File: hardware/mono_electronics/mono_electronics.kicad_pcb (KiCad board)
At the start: 4 copper layers, 190 x 148 mm, 181 parts, among them SW1 KMR2, U1 ESP32-S3FN8, Y1 L327S400H11L

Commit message: fix(mono): AON spine connectivity, VBUS decouple, DRC 0/0/73
- Join MCU AON east spine to translator bus on In2 to avoid ROW_01_Y crossing
  and prevent orphaned In1 stub from merging into GND on save.
- Route C_USB1 VBUS to existing USB In2 spine.
- Add drc_summary.py helper; document findings in LAST_CHANGES and cursor.md.

Co-authored-by: illiapliukhin <illiapliukhin@users.noreply.github.com>
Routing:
- net AON_3V3: track 98.6 -> 173.6 mm, vias 6 -> 10
- net GND: track 989.8 -> 915.7 mm, vias 52 -> 49
- net VBUS: track 50.0 -> 58.0 mm, vias 5 -> 6

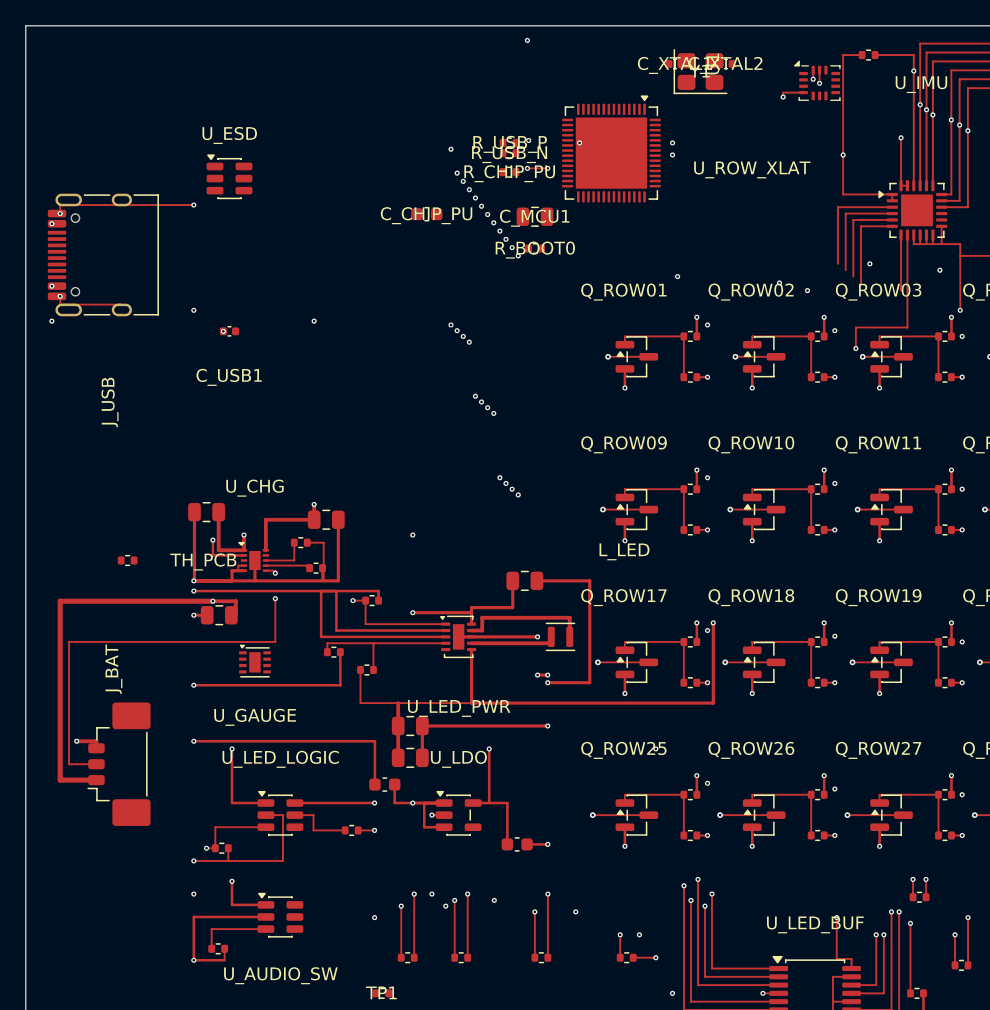
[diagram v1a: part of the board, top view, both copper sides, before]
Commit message: feat(mono): ESP32 pad remap, A* MCU grid router, 0-short grid pass
- Fix U1 pad map (SPICS0/GPIO6 NC; ROW_A0–A2 and AUDIO_EN GPIO remap)
- Remove illegal AON via in EP; placement for Y1/USB/crystal courtyards
- Add mcu_grid pipeline (dump → A* compute → apply complete nets only)
- Regenerated mono_electronics: 0 shorts/crossings, 46 unconnected with grid

Co-authored-by: illiapliukhin <illiapliukhin@users.noreply.github.com>
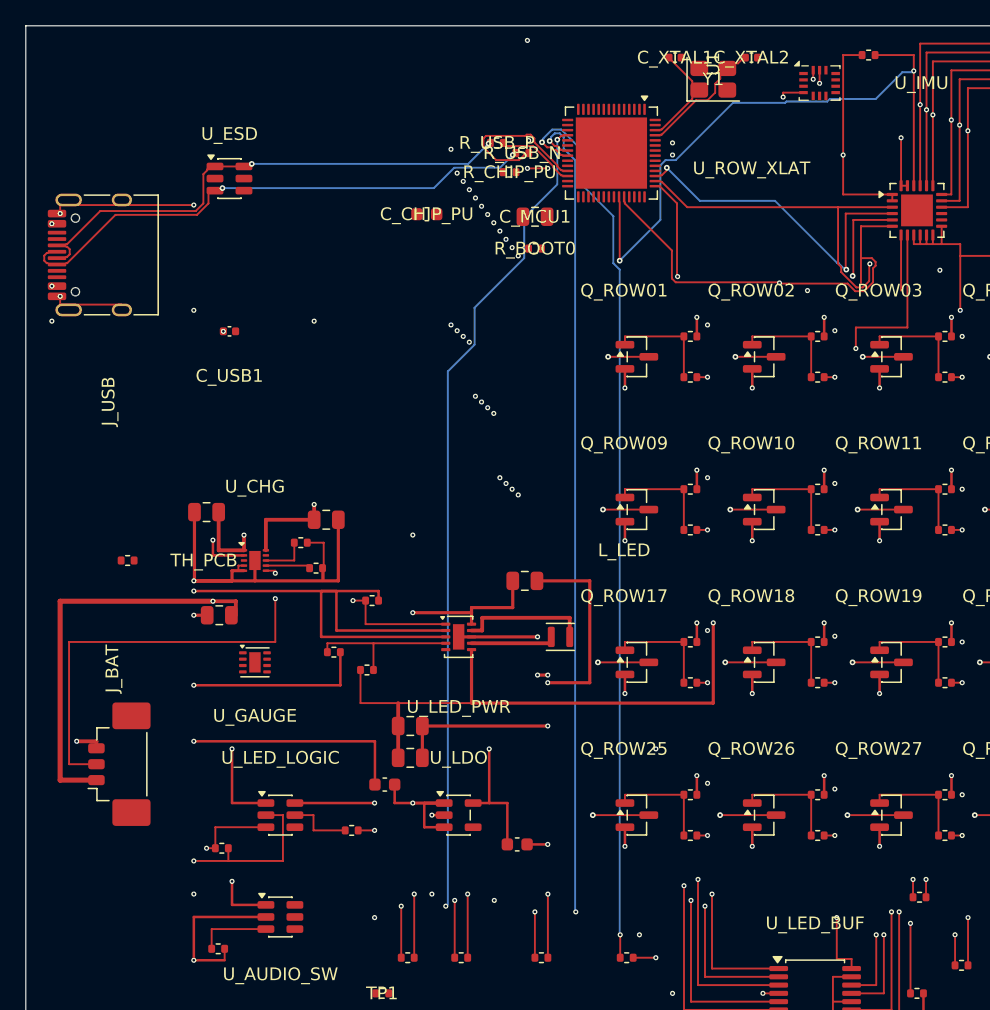
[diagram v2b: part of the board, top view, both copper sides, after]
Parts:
- moved C_XTAL2 2.06 mm to (57.0, 2.50)
- moved Y1 1.17 mm to (54.0, 4.20)
- moved R_USB_N 1.00 mm to (39.0, 10.0)
- moved R_USB_P 1.00 mm to (37.0, 9.20)
- moved C_XTAL1 0.50 mm to (51.0, 2.50)
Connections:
- U1 pad 11: GND -> (no net)
- U1 pad 23: ROW_A0 -> AUDIO_EN
- U1 pad 24: ROW_A1 -> (no net)
- U1 pad 27: ROW_A2 -> (no net)
- U1 pad 32: GND -> (no net)
- U1 pad 43: (no net) -> ROW_A2
- U1 pad 44: GND -> ROW_A0
- U1 pad 45: GND -> ROW_A1
- U1 pad 48: AUDIO_EN -> (no net)
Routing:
- net LED_OE_N: track 64.7 -> 133.7 mm, vias 5 -> 6
- net LED_CLK: track 68.1 -> 132.3 mm, vias 4 -> 5
- net LED_LE: track 77.6 -> 141.6 mm, vias 5 -> 6
- net USB_D_N: track 0.00 -> 38.9 mm, vias 0 -> 2
- net USB_D_P: track 0.00 -> 36.5 mm, vias 0 -> 2
- net ROW_XLAT_OE_N: track 156.0 -> 192.2 mm, vias 3 -> 4
- net ROW_A3: track 133.0 -> 159.6 mm
- net ROW_A0: track 92.8 -> 112.3 mm
- net ROW_A1: track 100.6 -> 118.6 mm, vias 2 -> 4
- net USB_D_N_MCU: track 0.00 -> 12.3 mm
- net XTAL_N: track 0.00 -> 7.86 mm
- net ROW_A2: track 135.9 -> 143.3 mm, vias 2 -> 3
- net AON_3V3: track 173.6 -> 166.3 mm, vias 10 -> 9
- net XTAL_P: track 0.00 -> 6.16 mm
- net USB_D_P_MCU: track 0.00 -> 5.41 mm

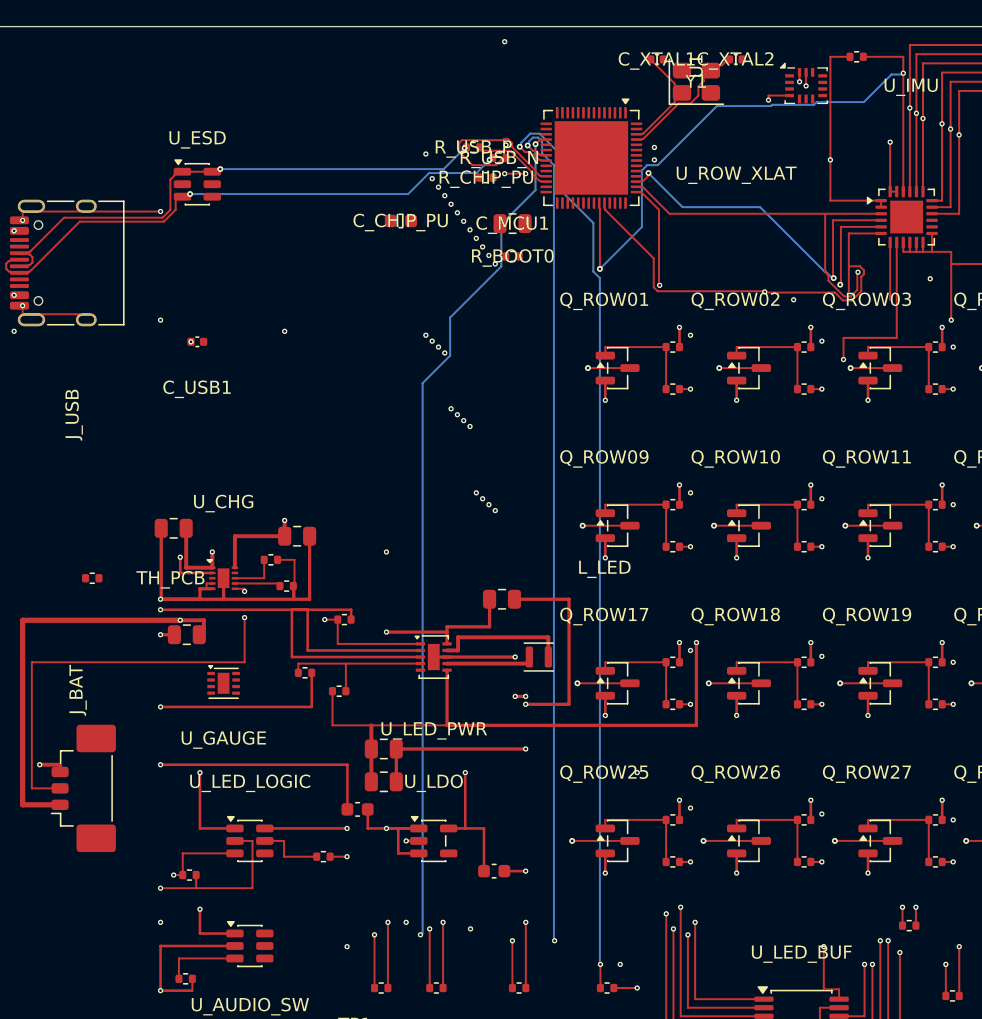
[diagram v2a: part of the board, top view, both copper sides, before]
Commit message: feat(mono): PathFinder grid negotiation and GND mesh helpers
Add pathfinder.py (history/rip-up/finish pass) behind MONO_PATHFINDER=1;
keep greedy router as default for 0-short apply. Extend grid Board with
recommit/uncommit and power track width. GND stitch/B.Cu mesh optional
(add_gnd_mesh false). Regenerated mono_electronics at 0/0/45 unconnected.

Co-authored-by: illiapliukhin <illiapliukhin@users.noreply.github.com>
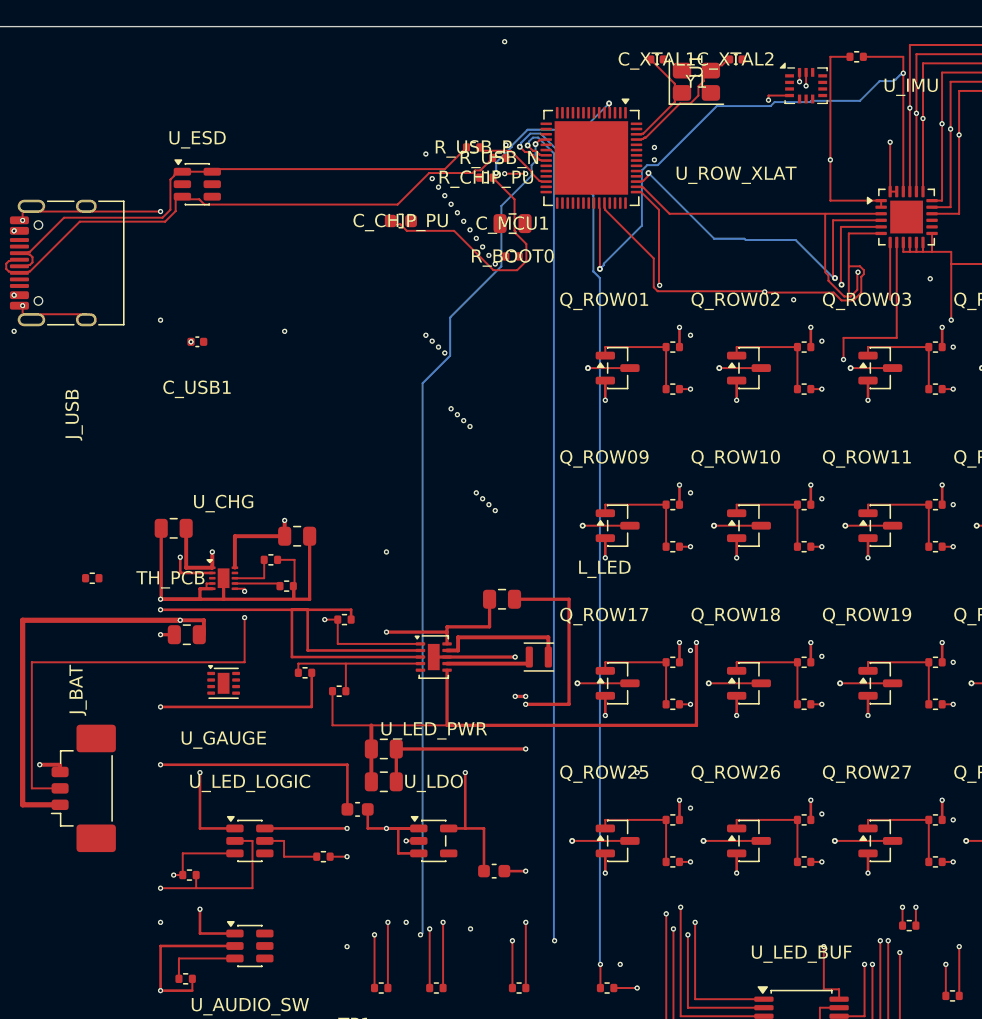
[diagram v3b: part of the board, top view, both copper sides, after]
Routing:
- net CHIP_PU: track 0.00 -> 30.4 mm, vias 0 -> 2
- net USB_D_N_MCU: track 12.3 -> 0.00 mm
- net USB_D_N: track 38.9 -> 39.4 mm, vias 2 -> 0
- net USB_D_P: track 36.5 -> 36.3 mm, vias 2 -> 0

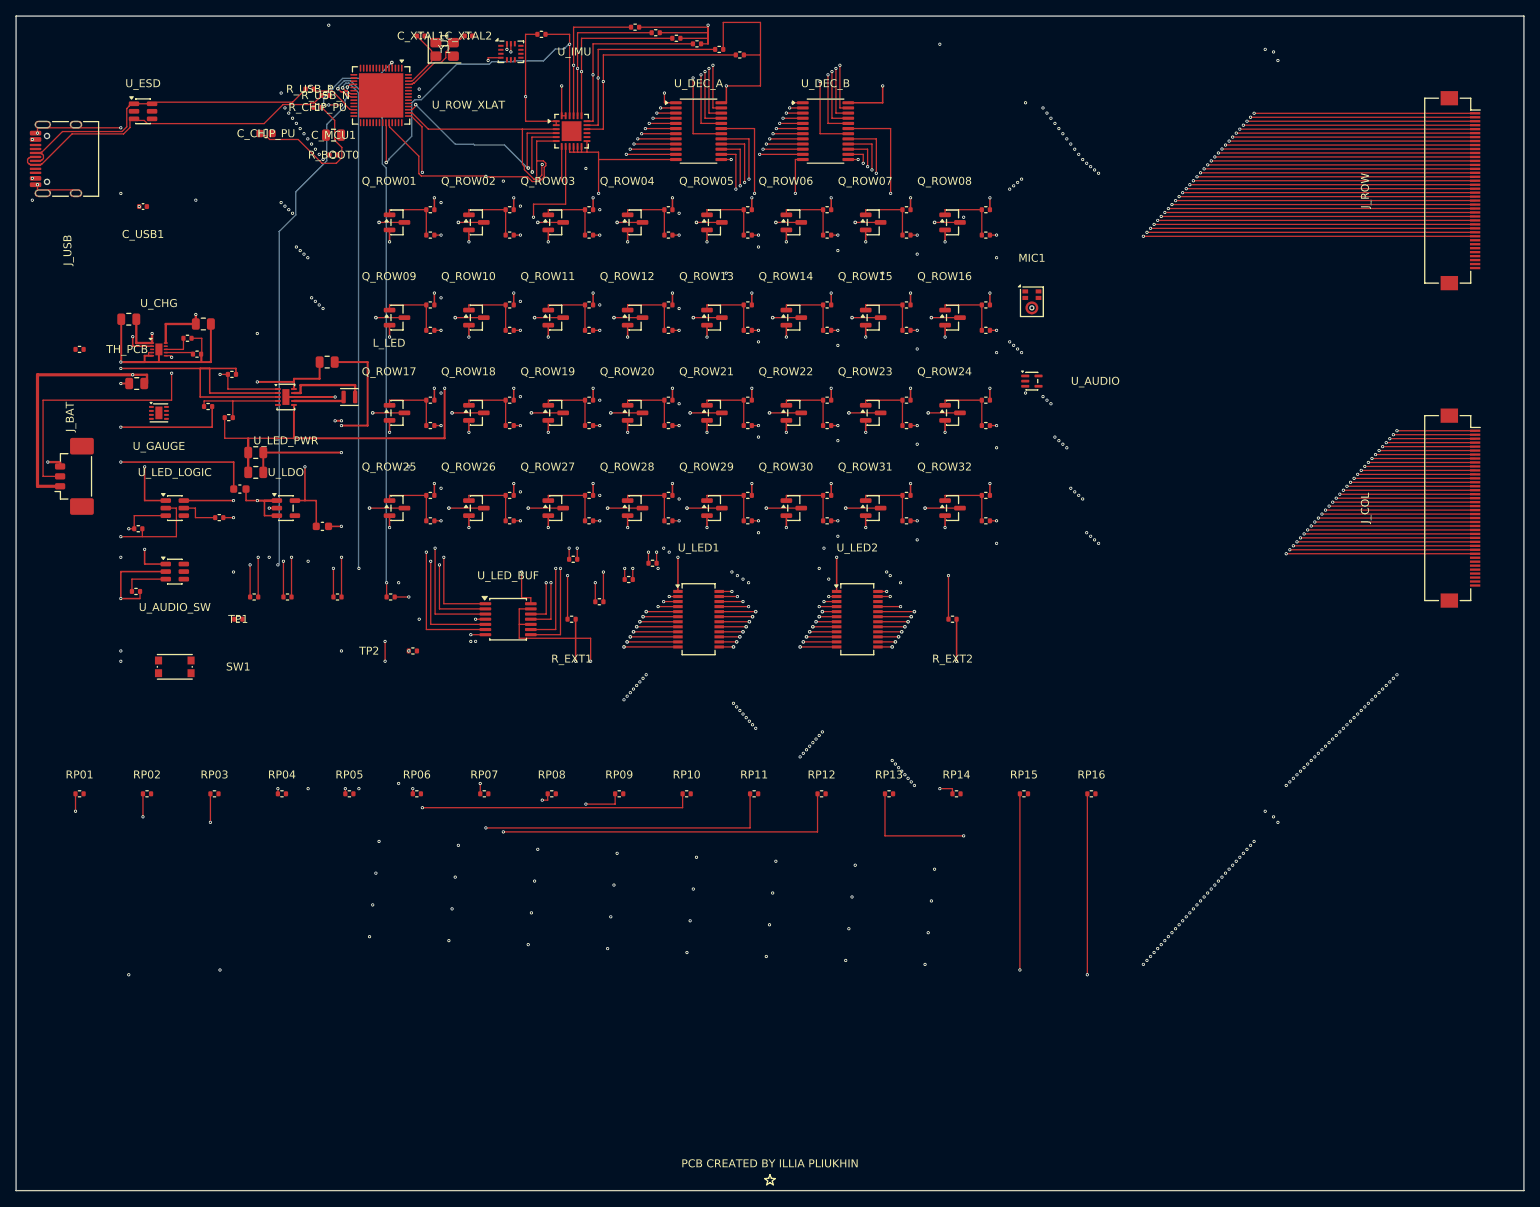
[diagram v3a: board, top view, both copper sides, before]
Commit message: feat(mono): PathFinder-first MCU grid with GPIO remap and GND refill
Run greedy and PathFinder compute, apply PathFinder when DRC gate passes
(0 shorts, 0 crossings) with more complete nets than greedy. Remap stubborn
nets to west/east pads (GPIO6/18/21/41/42), adjust USB series placement, add
In2/B GND zones filled via kicad-cli, and document the updated pin map.

Co-authored-by: illiapliukhin <illiapliukhin@users.noreply.github.com>
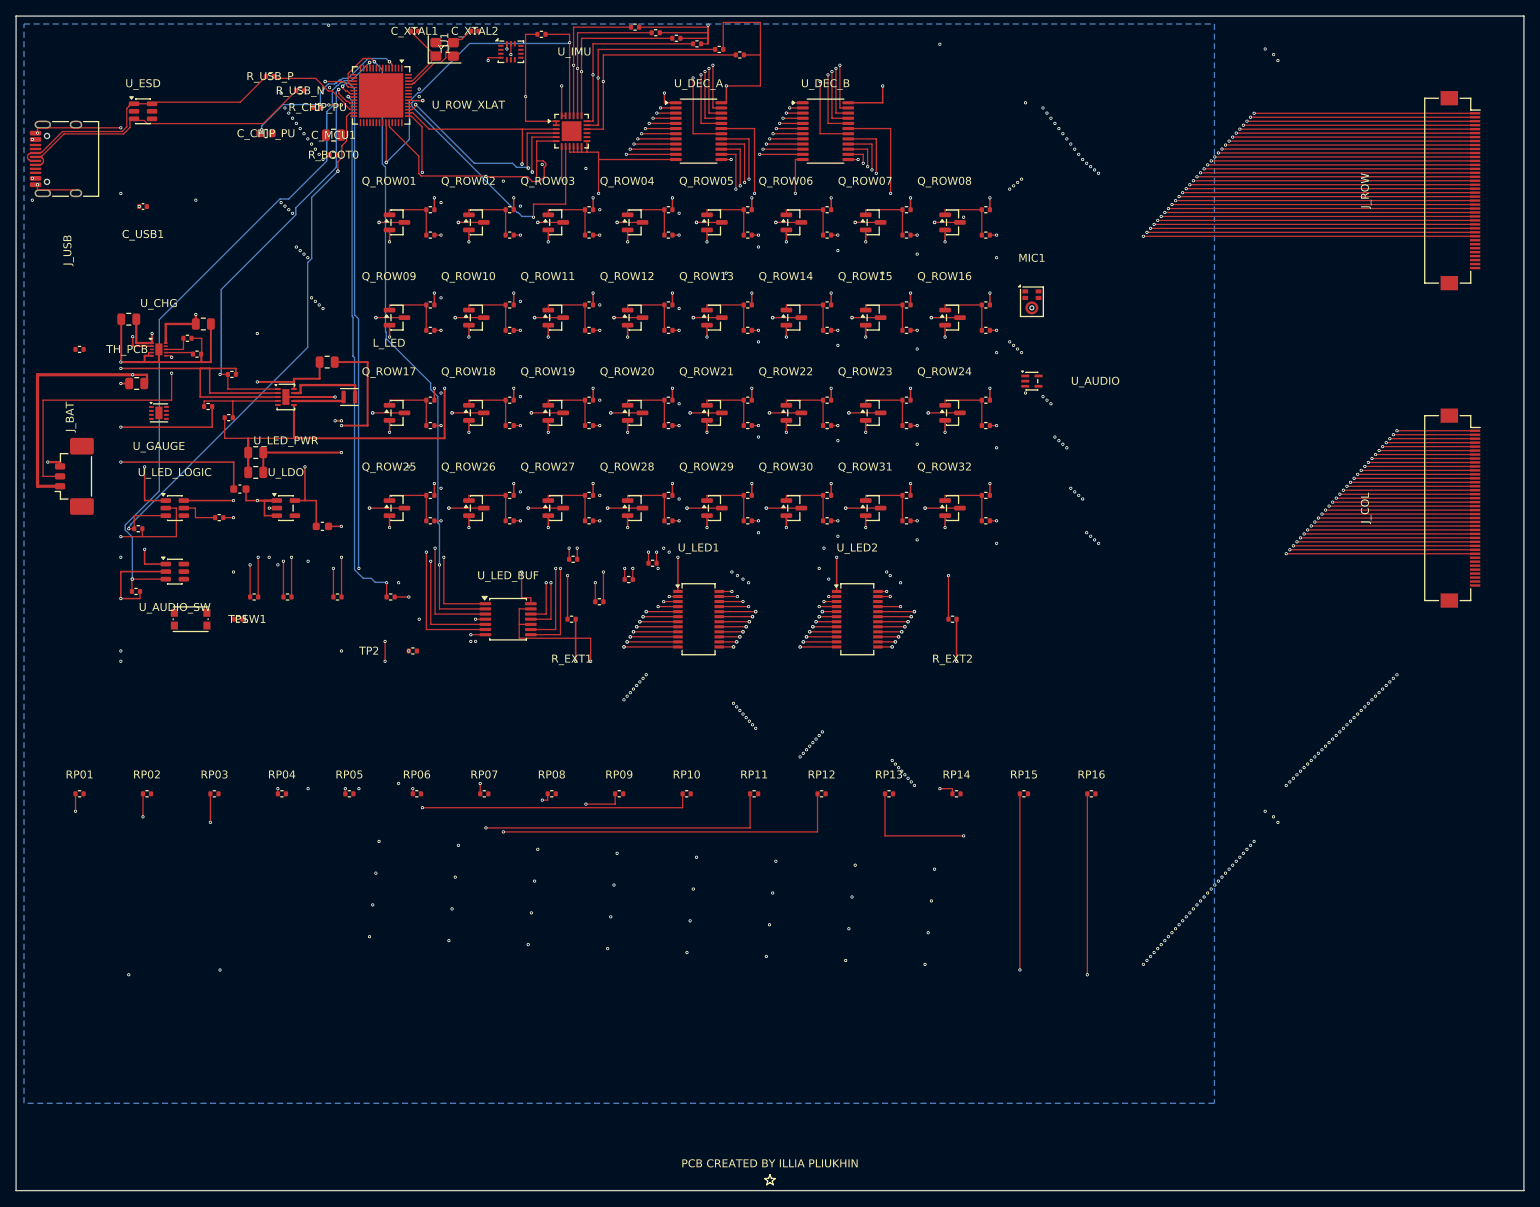
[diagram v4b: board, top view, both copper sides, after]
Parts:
- moved SW1 6.32 mm to (22.0, 76.0)
- moved R_USB_P 5.25 mm to (32.0, 7.60)
- moved R_USB_N 3.26 mm to (35.8, 9.40)
- moved C_XTAL1 1.00 mm to (50.2, 1.90)
- moved C_XTAL2 1.00 mm to (57.8, 1.90)
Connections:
- U1 pad 11: (no net) -> AUDIO_EN
- U1 pad 23: AUDIO_EN -> (no net)
- U1 pad 24: (no net) -> LED_EN
- U1 pad 27: (no net) -> LED_LOGIC_EN
- U1 pad 39: DEC_A_EN_N -> (no net)
- U1 pad 40: DEC_B_EN_N -> (no net)
- U1 pad 41: LED_EN -> (no net)
- U1 pad 42: LED_LOGIC_EN -> (no net)
- U1 pad 47: (no net) -> DEC_A_EN_N
- U1 pad 48: (no net) -> DEC_B_EN_N
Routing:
- net AUDIO_EN: track 5.81 -> 85.7 mm, vias 0 -> 2
- net LED_SDI: track 71.9 -> 136.8 mm, vias 5 -> 6
- net LED_LOGIC_EN: track 206.1 -> 269.9 mm, vias 3 -> 4
- net LED_EN: track 207.2 -> 251.6 mm, vias 3 -> 4
- net DEC_B_EN_N: track 160.3 -> 184.7 mm, vias 3 -> 4
- net CHIP_PU: track 30.4 -> 21.6 mm, vias 2 -> 3
- net LED_CLK: track 132.3 -> 140.4 mm
- net USB_D_P_MCU: track 5.41 -> 11.1 mm
- net ROW_A0: track 112.3 -> 107.6 mm, vias 2 -> 3
- net USB_D_P: track 36.3 -> 32.0 mm
- net LED_OE_N: track 133.8 -> 129.5 mm
- net USB_D_N: track 39.4 -> 36.0 mm
- net XTAL_N: track 7.86 -> 8.91 mm
- net XTAL_P: track 6.16 -> 7.09 mm
- net ROW_XLAT_OE_N: track 192.2 -> 193.0 mm
- added copper zone on B.Cu, net GND
- added copper zone on In2.Cu, net GND
